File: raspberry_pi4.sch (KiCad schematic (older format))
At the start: 1 part, among them J12 Conn_02x20_Odd_Even

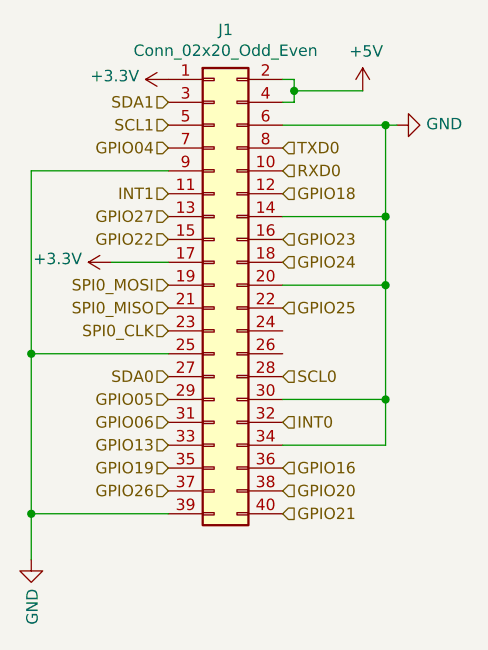
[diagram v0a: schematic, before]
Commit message: Conexão entre os componentes. Correção da lib do buck-boost. Separação do 3v3 da raspberry e do 3v3 do regulador
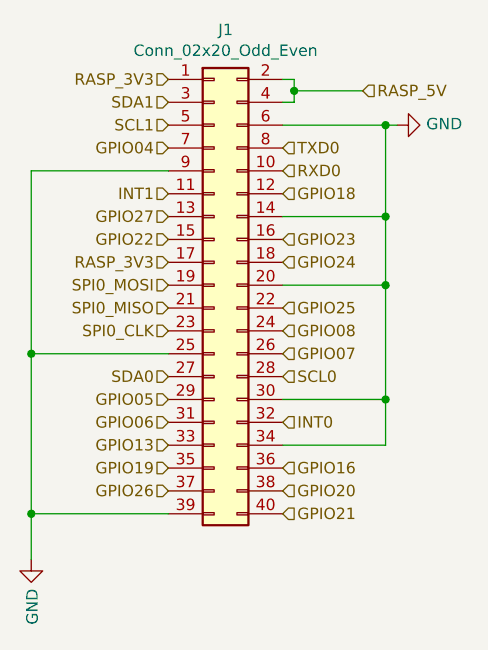
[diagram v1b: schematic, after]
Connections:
- net GPIO08: now reaches J12.24 (Pin_24)
- net GPIO07: now reaches J12.26 (Pin_26)
- net +3V3 renamed RASP_3V3
- net +5V renamed RASP_5V
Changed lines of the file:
@@
 Wire Wire Line
 	4750 2200 4750 2250
-$Comp
-L power:+5V #PWR?
-U 1 1 61DB6E79
-P 5050 2200
-AR Path="/61C25AB3/61DB6E79" Ref="#PWR?"  Part="1"
-AR Path="/61DA8240/61DB6E79" Ref="#PWR0121"  Part="1"
-AR Path="/61DBD0E2/61DB6E79" Ref="#PWR0101"  Part="1"
-F 0 "#PWR0101" H 5050 2050 50  0001 C CNN
-F 1 "+5V" H 5065 2373 50  0000 C CNN
-F 2 "" H 5050 2200 50  0001 C CNN
-F 3 "" H 5050 2200 50  0001 C CNN
-	1    5050 2200
-	1    0    0    -1
-$EndComp
 Wire Wire Line
 	4750 2200 5050 2200
@@
 GPIO04
 $Comp
-L power:+3.3V #PWR0103
-U 1 1 620AE1C8
-P 3950 2950
-F 0 "#PWR0103" H 3950 2800 50  0001 C CNN
-F 1 "+3.3V" V 3965 3078 50  0000 L CNN
-F 2 "" H 3950 2950 50  0001 C CNN
-F 3 "" H 3950 2950 50  0001 C CNN
-	1    3950 2950
-	0    -1   -1   0
-$EndComp
-$Comp
-L power:+3.3V #PWR0104
-U 1 1 620B0849
-P 4200 2150
-F 0 "#PWR0104" H 4200 2000 50  0001 C CNN
-F 1 "+3.3V" V 4215 2278 50  0000 L CNN
-F 2 "" H 4200 2150 50  0001 C CNN
-F 3 "" H 4200 2150 50  0001 C CNN
-	1    4200 2150
-	0    -1   -1   0
-$EndComp
-$Comp
 L power:GND #PWR0105
 U 1 1 620B362D
@@
 	3600 3350 3600 2550
 Connection ~ 3600 4050
-Wire Wire Line
-	4200 2950 3950 2950
 Wire Wire Line
 	4700 2350 5150 2350
@@
 Text HLabel 4200 3650 0    50   Input ~ 0
 GPIO06
+Text HLabel 5050 2200 2    50   Input ~ 0
+RASP_5V
+Text HLabel 4200 2150 0    50   Input ~ 0
+RASP_3V3
+Text HLabel 4200 2950 0    50   Input ~ 0
+RASP_3V3
+Text HLabel 4700 3250 2    50   Input ~ 0
+GPIO08
+Text HLabel 4700 3350 2    50   Input ~ 0
+GPIO07
 $EndSCHEMATC
